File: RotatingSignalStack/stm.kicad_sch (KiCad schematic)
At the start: 1 part, among them IC2 STM32H562RIT6

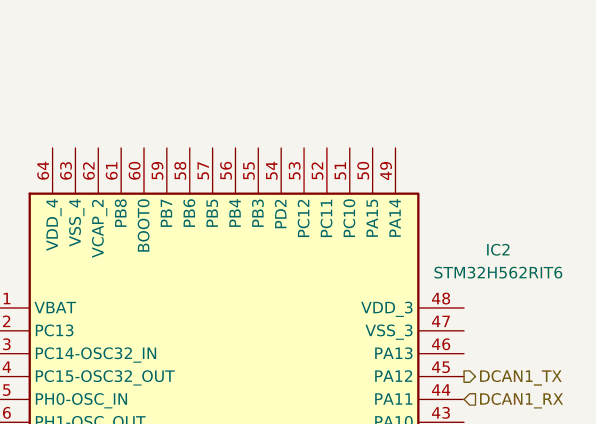
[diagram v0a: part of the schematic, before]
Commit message: Added motor connections to STM
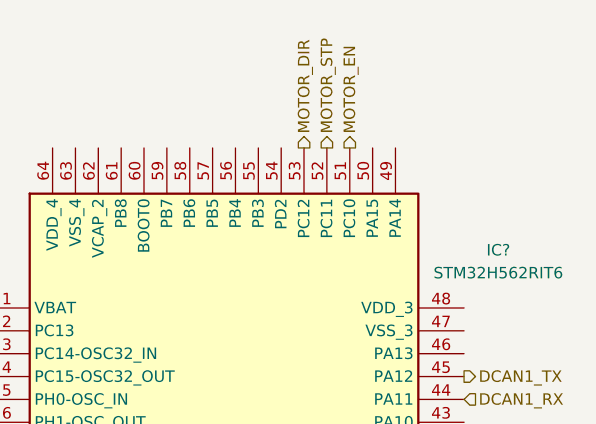
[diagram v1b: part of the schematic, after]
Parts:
- renumbered IC2 to IC?
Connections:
- net MOTOR_EN: now reaches IC?.51 (PC10)
- net MOTOR_STP: now reaches IC?.52 (PC11)
- net MOTOR_DIR: now reaches IC?.53 (PC12)
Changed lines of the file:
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@@
+		)
+	)
+	(hierarchical_label "MOTOR_STP"
+		(shape output)
+		(at 153.67 60.96 90)
+		(effects
+			(font
+				(size 1.27 1.27)
+			)
+			(justify left)
 		)
 	)
@@
 		)
 	)
+	(hierarchical_label "MOTOR_DIR"
+		(shape output)
+		(at 151.13 60.96 90)
+		(effects
+			(font
+				(size 1.27 1.27)
+			)
+			(justify left)
+		)
+	)
 	(hierarchical_label "TX_D1"
 		(shape input)
 		(at 168.91 109.22 0)
+		(effects
+			(font
+				(size 1.27 1.27)
+			)
+			(justify left)
+		)
+	)
+	(hierarchical_label "MOTOR_EN"
+		(shape output)
+		(at 156.21 60.96 90)
 		(effects
 			(font
@@
 		(dnp no)
 		(fields_autoplaced yes)
-		(property "Reference" "IC2"
+		(property "Reference" "IC?"
 			(at 172.72 72.3198 0)
 			(effects
@@
 		)
 		(instances
+			(project "stm"
+				(path "/47894d99-59eb-47c3-8dc1-da6679d60b45"
+					(reference "IC?")
+					(unit 1)
+				)
+			)
 			(project "RotatingSignalStack"
 				(path "/fbbbfa89-3c28-4cf8-856b-66ca7308742c/85f5c4be-2744-4dc6-8792-10e4391fb2cb"
@@
 		)
 	)
+	(sheet_instances
+		(path "/"
+			(page "1")
+		)
+	)
+	(embedded_fonts no)
 )

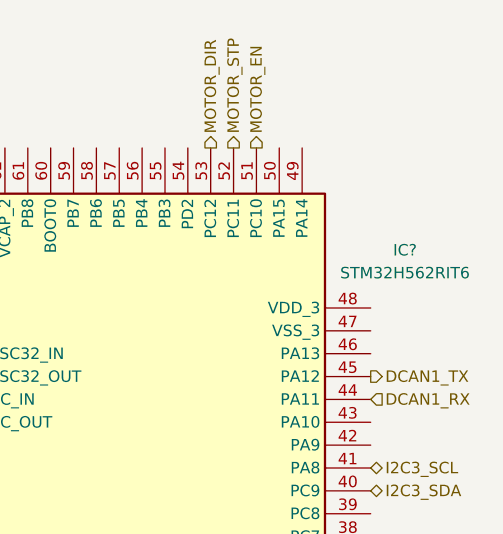
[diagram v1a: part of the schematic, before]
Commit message: Added motor connectors
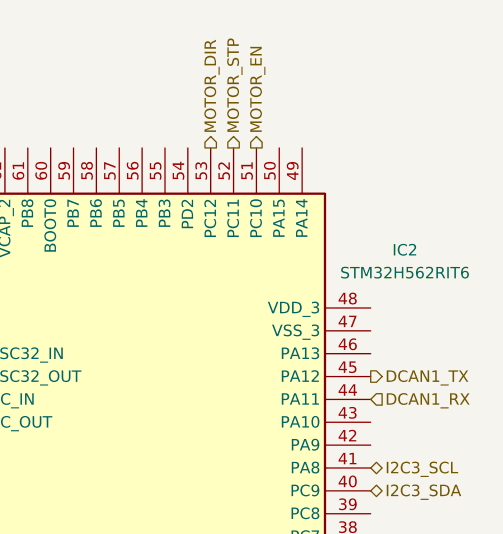
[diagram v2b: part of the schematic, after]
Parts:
- gave numbers to parts that had none: 1
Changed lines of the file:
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@@
 		(dnp no)
 		(fields_autoplaced yes)
-		(property "Reference" "IC?"
+		(property "Reference" "IC2"
 			(at 172.72 72.3198 0)
 			(effects

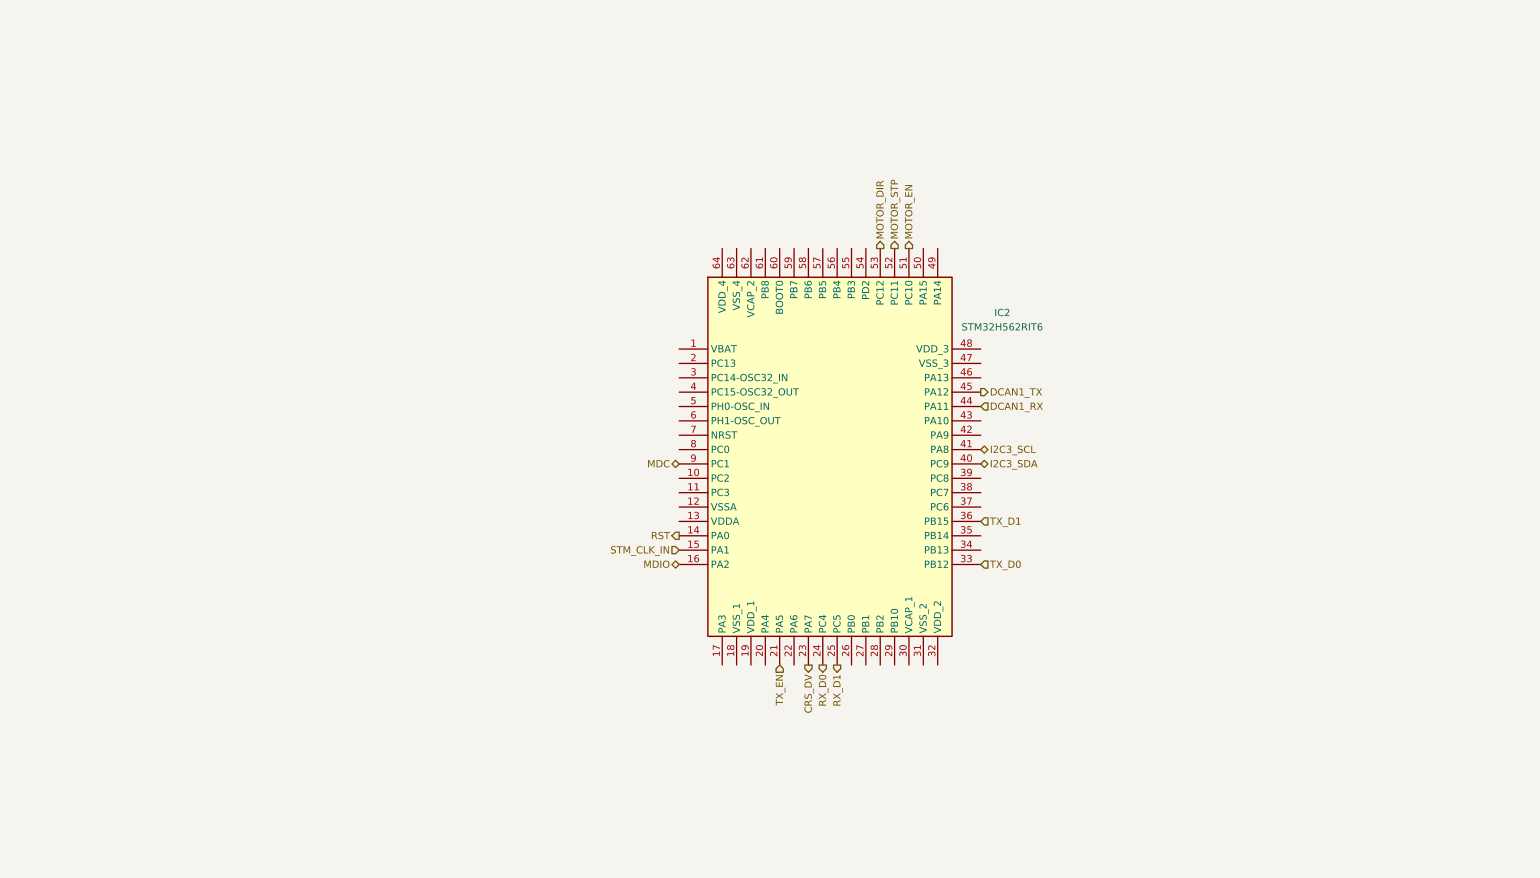
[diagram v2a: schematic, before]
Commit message: STM design and ESD protection
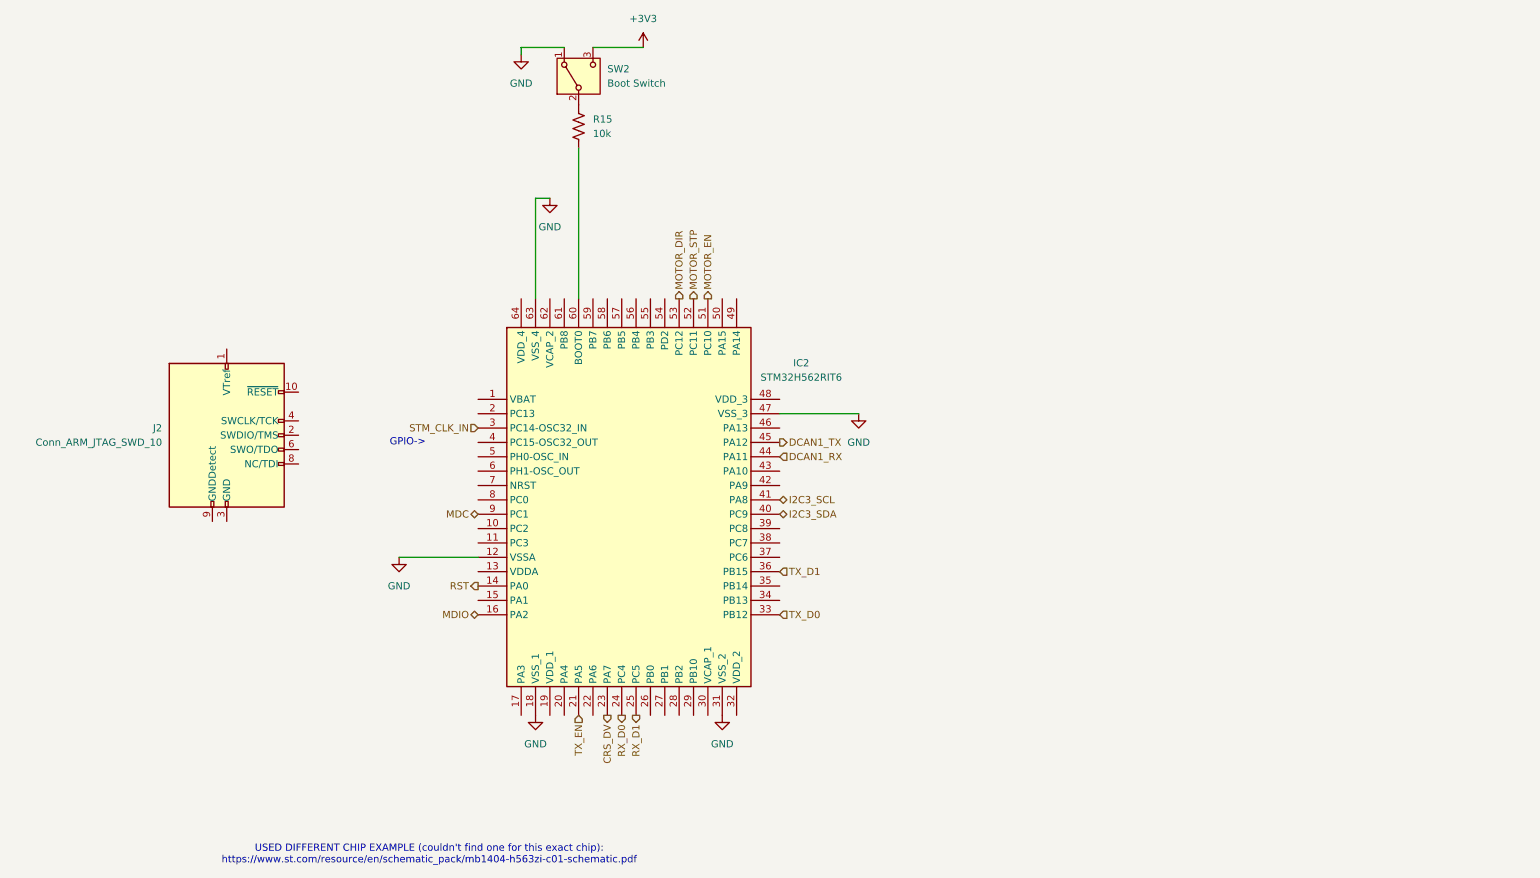
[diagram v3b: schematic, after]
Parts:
- added J2: Conn_ARM_JTAG_SWD_10, symbol Connector:Conn_ARM_JTAG_SWD_10
- added R15: 10k, symbol Device:R_US
- added SW2: Boot Switch, Button_Switch_THT:SW_Slide_SPDT_Angled_CK_OS102011MA1Q, symbol Switch:SW_SPDT
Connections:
- net STM_CLK_IN: now also IC2.3 (PC14-OSC32_IN); no longer IC2.15 (PA1)
- net GND: now reaches IC2.12 (VSSA)
- net GND: now also IC2.18 (VSS_1), IC2.31 (VSS_2), IC2.47 (VSS_3), IC2.63 (VSS_4), SW2.1 (A)
- net at IC2.60 (BOOT0): now also R15.1
- new net: R15.2, SW2.2 (B)
- new net: J2.3 (GND), J2.5 (GND)
- new net +3V3: SW2.3 (C)
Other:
- note added: "GPIO->"
- note added: "USED DIFFERENT CHIP EXAMPLE (couldn't find one for this exact chip): https://www.st.com/resource/en/schematic_pack/mb1404-h563zi-c01-schematic.pdf"
- moved on the sheet: IC2

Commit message: STM designed (mostly), ESD and pin linking next
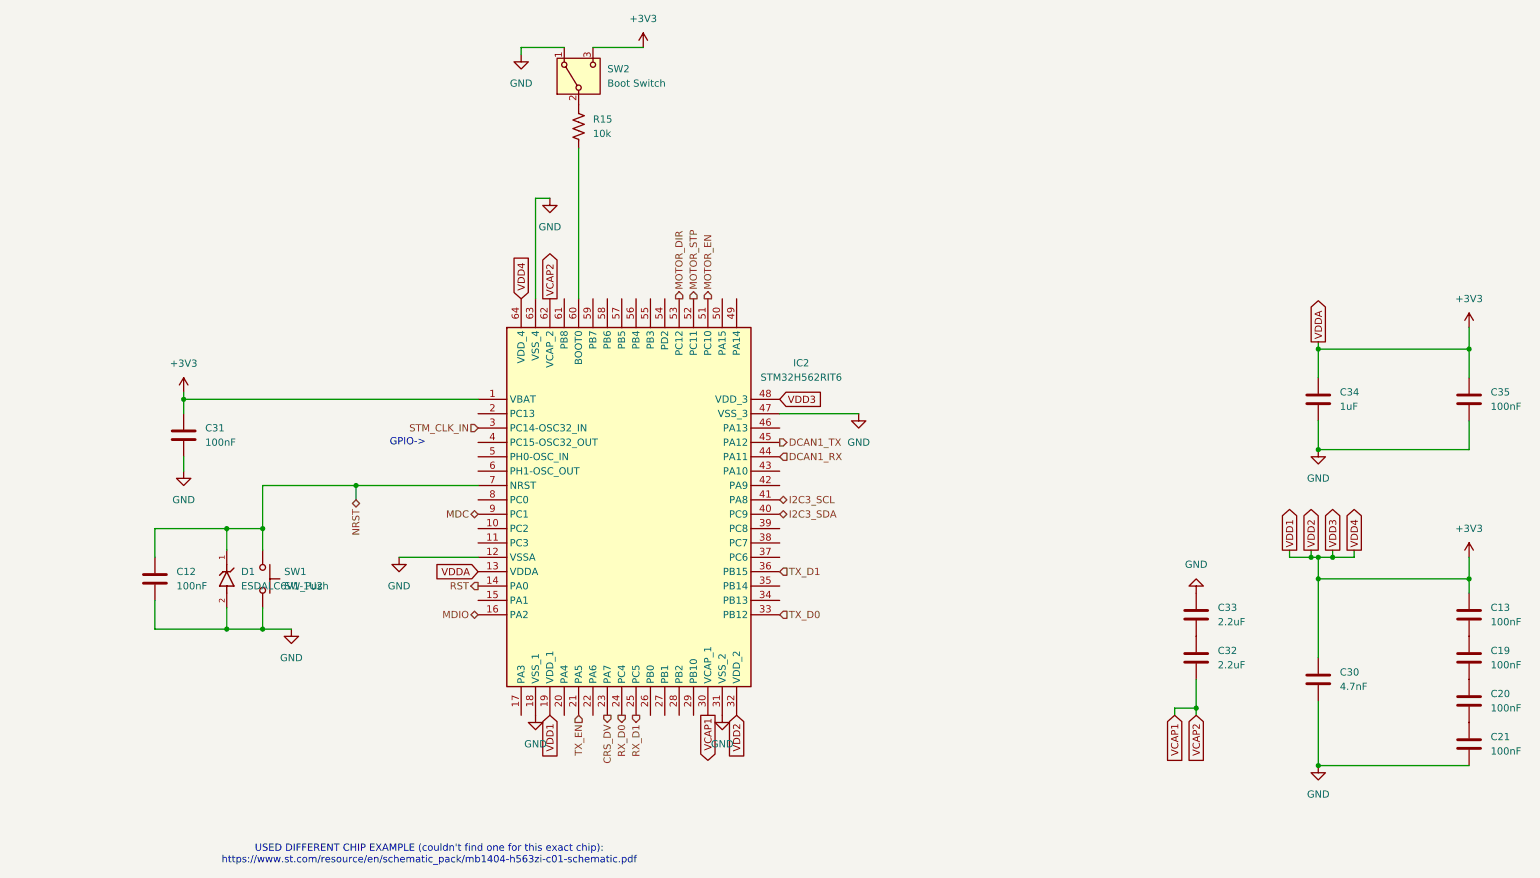
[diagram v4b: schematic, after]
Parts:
- removed J2: Conn_ARM_JTAG_SWD_10, symbol Connector:Conn_ARM_JTAG_SWD_10
- added C12, C13, C19, C20, C21, C31, C35: 100nF, symbol Device:C
- added C30: 4.7nF, symbol Device:C
- added C32, C33: 2.2uF, symbol Device:C
- added C34: 1uF, symbol Device:C
- added D1: ESDALC6V1-1U2, ESDALC6V1-1U2:DIODE_ESDALC6V1-1U2, symbol ESDALC6V1-1U2:ESDALC6V1-1U2
- added SW1: SW_Push, symbol Switch:SW_Push
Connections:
- net +3V3: now also IC2.1 (VBAT), IC2.13 (VDDA), IC2.19 (VDD_1), IC2.32 (VDD_2), IC2.48 (VDD_3), IC2.64 (VDD_4), C13.1, C30.1, C31.1, C34.1, C35.1
- net GND: now also C12.2, C21.2, C30.2, C31.2, C33.1, C34.2, C35.2, D1.2, SW1.2
- net VCAP1: now reaches IC2.30 (VCAP_1)
- net VCAP1: now also IC2.62 (VCAP_2), C32.2
- net NRST: now reaches IC2.7 (NRST)
- net NRST: now also C12.1, D1.1, SW1.1
- new net: C13.2, C19.1
- new net: C19.2, C20.1
- new net: C20.2, C21.1
- new net: C32.1, C33.2

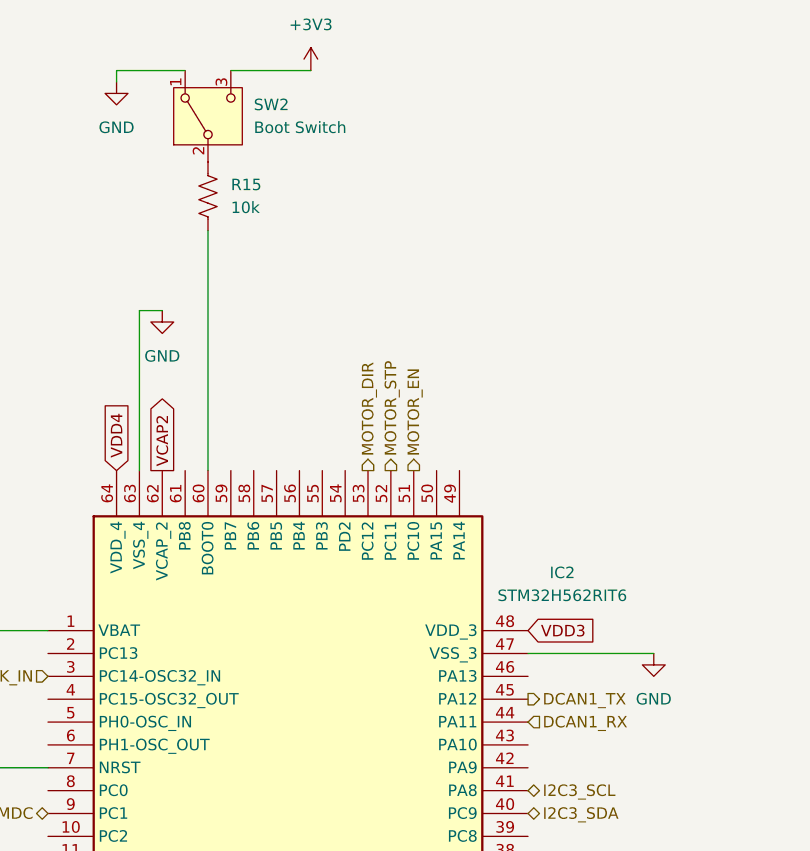
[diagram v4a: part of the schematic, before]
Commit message: Added Compass ESD protection
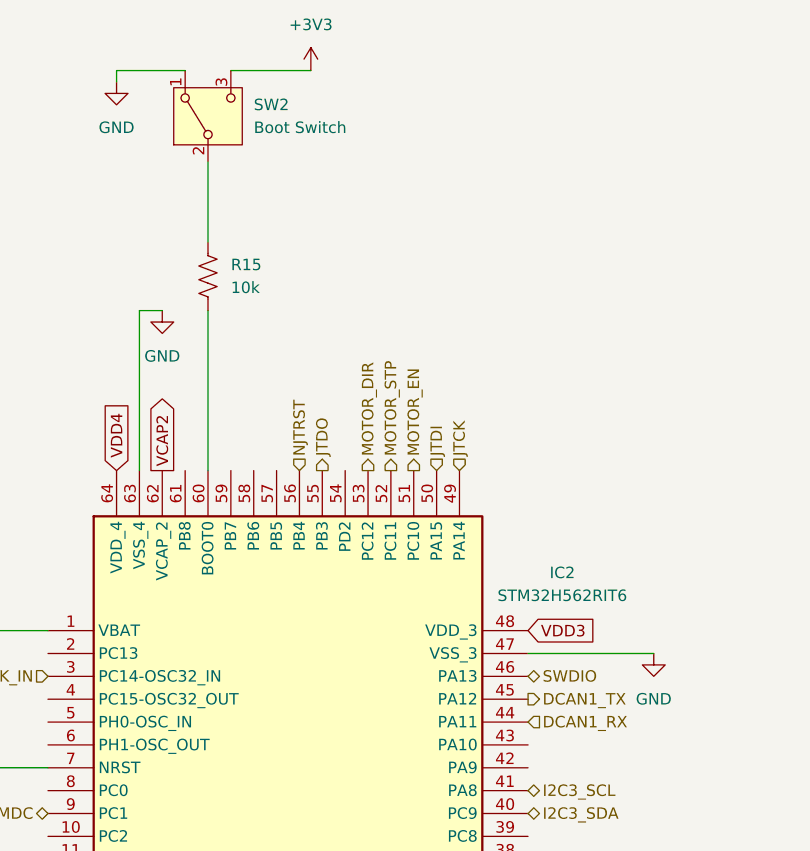
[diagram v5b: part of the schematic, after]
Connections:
- net SWDIO: now reaches IC2.46 (PA13)
- net JTCK: now reaches IC2.49 (PA14)
- net JTDI: now reaches IC2.50 (PA15)
- net JTDO: now reaches IC2.55 (PB3)
- net NJTRST: now reaches IC2.56 (PB4)
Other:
- moved on the sheet: R15
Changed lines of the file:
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@@
+	(wire
+		(pts
+			(xy 97.79 44.45) (xy 97.79 35.56)
+		)
+		(stroke
+			(width 0)
+			(type default)
+		)
+	)
 	(wire
 		(pts
@@
 	(wire
 		(pts
-			(xy 97.79 43.18) (xy 97.79 69.85)
+			(xy 97.79 52.07) (xy 97.79 69.85)
 		)
 		(stroke
@@
 		)
 	)
+	(hierarchical_label "JTDI"
+		(shape input)
+		(at 123.19 69.85 90)
+		(effects
+			(font
+				(size 1.27 1.27)
+			)
+			(justify left)
+		)
+	)
 	(hierarchical_label "MOTOR_STP"
 		(shape output)
@@
 		)
 	)
+	(hierarchical_label "JTDO"
+		(shape output)
+		(at 110.49 69.85 90)
+		(effects
+			(font
+				(size 1.27 1.27)
+			)
+			(justify left)
+		)
+	)
+	(hierarchical_label "JTCK"
+		(shape input)
+		(at 125.73 69.85 90)
+		(effects
+			(font
+				(size 1.27 1.27)
+			)
+			(justify left)
+		)
+	)
 	(hierarchical_label "STM_CLK_IN"
 		(shape input)
@@
 		)
 	)
+	(hierarchical_label "NJTRST"
+		(shape input)
+		(at 107.95 69.85 90)
+		(effects
+			(font
+				(size 1.27 1.27)
+			)
+			(justify left)
+		)
+	)
 	(hierarchical_label "RX_D1"
 		(shape output)
@@
 			)
 			(justify right)
+		)
+	)
+	(hierarchical_label "SWDIO"
+		(shape bidirectional)
+		(at 133.35 92.71 0)
+		(effects
+			(font
+				(size 1.27 1.27)
+			)
+			(justify left)
 		)
 	)
@@
 	(symbol
 		(lib_id "Device:R_US")
-		(at 97.79 39.37 180)
+		(at 97.79 48.26 180)
 		(unit 1)
 		(exclude_from_sim no)
@@
 		(fields_autoplaced yes)
 		(property "Reference" "R15"
-			(at 100.33 38.0999 0)
+			(at 100.33 46.9899 0)
 			(effects
 				(font
@@
 		)
 		(property "Value" "10k"
-			(at 100.33 40.6399 0)
+			(at 100.33 49.5299 0)
 			(effects
 				(font
@@
 		)
 		(property "Footprint" ""
-			(at 96.774 39.116 90)
+			(at 96.774 48.006 90)
 			(effects
 				(font
@@
 		)
 		(property "Datasheet" "~"
-			(at 97.79 39.37 0)
+			(at 97.79 48.26 0)
 			(effects
 				(font
@@
 		)
 		(property "Description" "Resistor, US symbol"
-			(at 97.79 39.37 0)
-			(effects
-				(font
+			(at 97.79 48.26 0)
+			(effects
+				(font

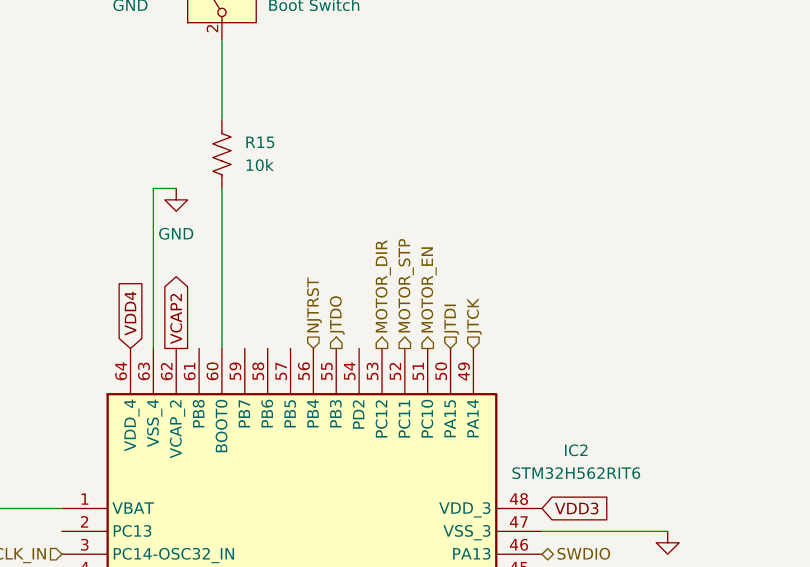
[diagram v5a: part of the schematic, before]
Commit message: Added Motor connector CAN
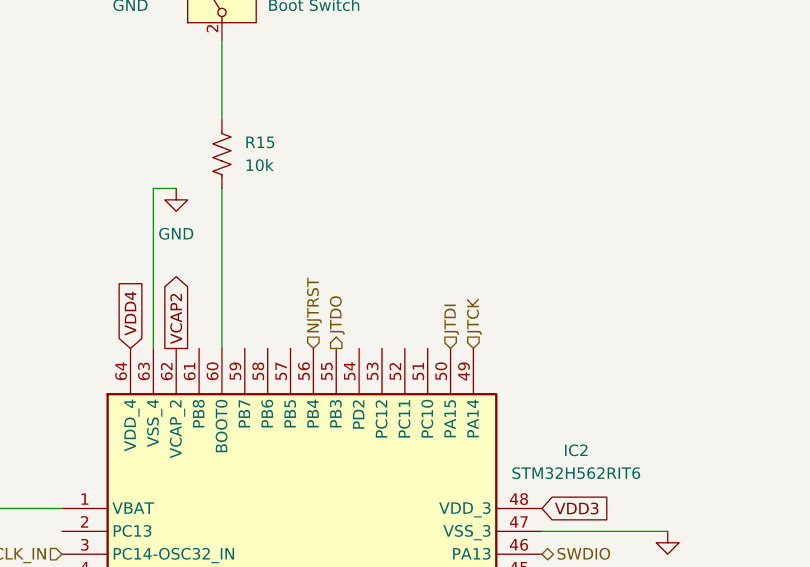
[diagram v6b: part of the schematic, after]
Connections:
- net MOTOR_DIR: no longer names the net of IC2.53 (PC12)
- net MOTOR_EN: no longer names the net of IC2.51 (PC10)
- net MOTOR_STP: no longer names the net of IC2.52 (PC11)
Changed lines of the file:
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@@
-		)
-	)
-	(hierarchical_label "MOTOR_STP"
-		(shape output)
-		(at 118.11 69.85 90)
-		(effects
-			(font
-				(size 1.27 1.27)
-			)
-			(justify left)
 		)
 	)
@@
 		)
 	)
-	(hierarchical_label "MOTOR_DIR"
-		(shape output)
-		(at 115.57 69.85 90)
-		(effects
-			(font
-				(size 1.27 1.27)
-			)
-			(justify left)
-		)
-	)
 	(hierarchical_label "TX_D1"
 		(shape input)
@@
 		(effects
 			(font
-				(size 1.27 1.27)
-			)
-			(justify left)
-		)
-	)
-	(hierarchical_label "MOTOR_EN"
-		(shape output)
-		(at 120.65 69.85 90)
-		(effects
-			(font
